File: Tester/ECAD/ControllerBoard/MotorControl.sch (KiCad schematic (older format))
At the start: 16 parts, among them J2 Conn_01x02_Male, J3 Conn_01x02_Male, J4 Conn_01x02_Male, J5 Conn_01x02_Male, U3 DRV8833PW, U4 DRV8833PW

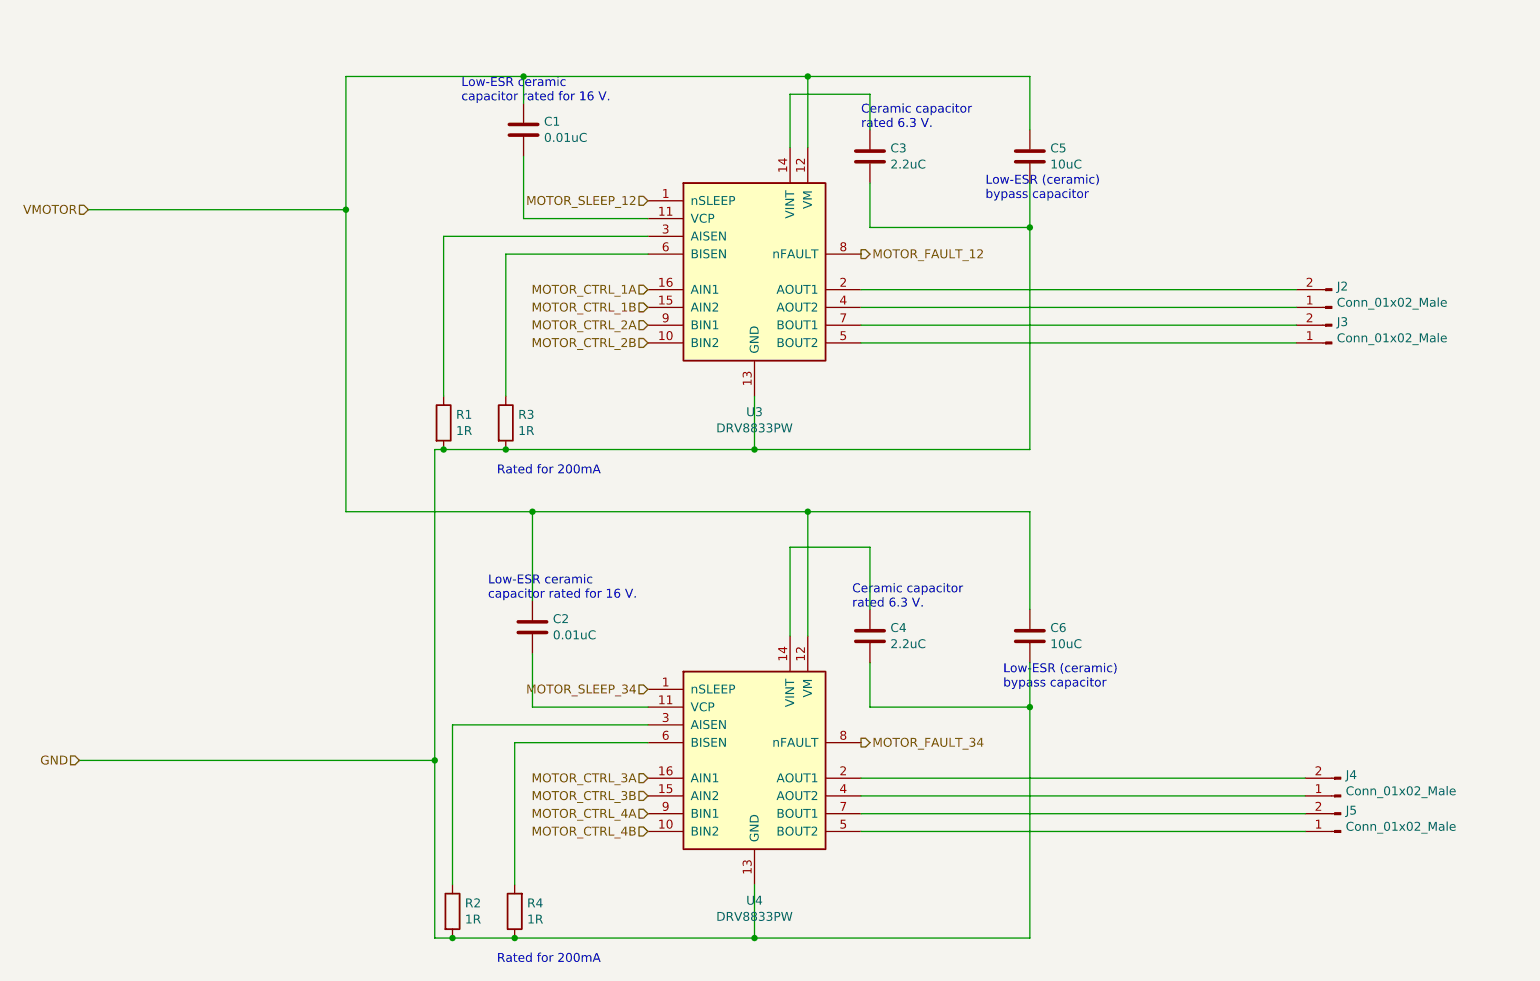
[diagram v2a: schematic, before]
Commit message: Progressed circuit layout.
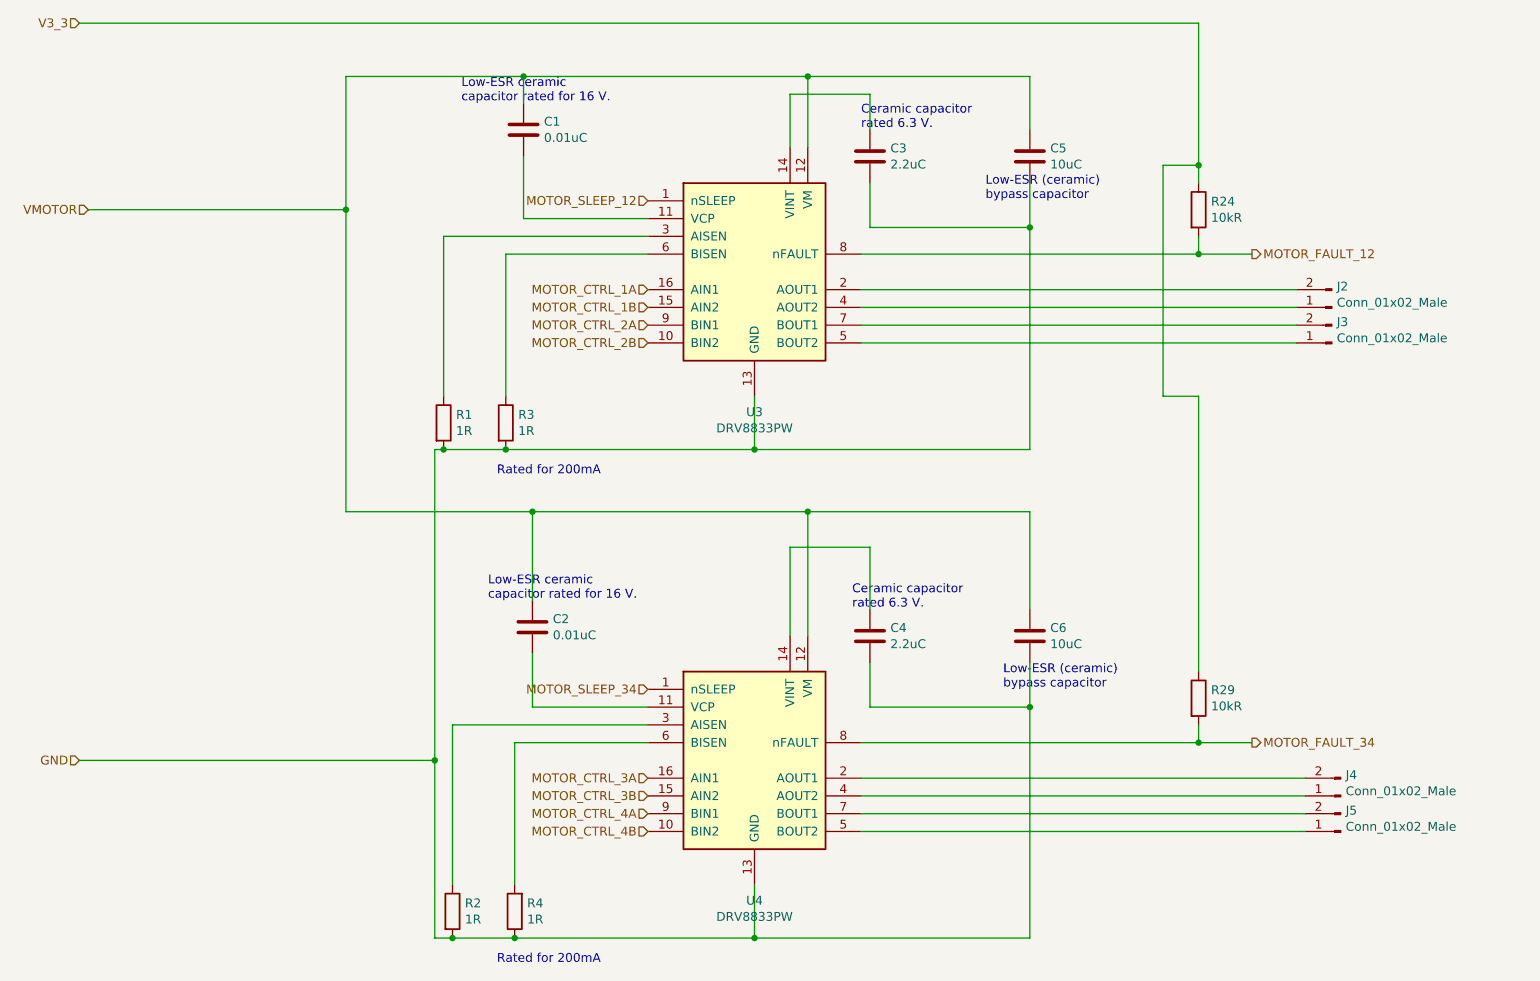
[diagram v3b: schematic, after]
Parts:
- added R24, R29: 10kR, Resistor_SMD:R_0805_2012Metric_Pad1.15x1.40mm_HandSolder, symbol Device:R
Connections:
- net MOTOR_FAULT_12: now also R24.2
- net MOTOR_FAULT_34: now also R29.2
- new net V3_3: R24.1, R29.1
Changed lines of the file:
@@
 Text Notes 6400 4200 0    50   ~ 0
 Ceramic capacitor\nrated 6.3 V.
-Text HLabel 6450 2200 2    50   Output ~ 0
+Text HLabel 8650 2200 2    50   Output ~ 0
 MOTOR_FAULT_12
-Text HLabel 6450 4950 2    50   Output ~ 0
+Text HLabel 8650 4950 2    50   Output ~ 0
 MOTOR_FAULT_34
 Text HLabel 5250 1900 0    50   Input ~ 0
@@
 Wire Wire Line
 	8950 5450 6450 5450
+$Comp
+L Device:R R29
+U 1 1 5E624B95
+P 8350 4700
+F 0 "R29" H 8420 4746 50  0000 L CNN
+F 1 "10kR" H 8420 4655 50  0000 L CNN
+F 2 "Resistor_SMD:R_0805_2012Metric_Pad1.15x1.40mm_HandSolder" V 8280 4700 50  0001 C CNN
+F 3 "~" H 8350 4700 50  0001 C CNN
+F 4 "RC0805FR-0710KL" H 8350 4700 50  0001 C CNN "Manufacturer Part Number"
+	1    8350 4700
+	1    0    0    -1
+$EndComp
+Wire Wire Line
+	6450 4950 8350 4950
+Wire Wire Line
+	8350 4850 8350 4950
+Connection ~ 8350 4950
+Wire Wire Line
+	8350 4950 8650 4950
+$Comp
+L Device:R R24
+U 1 1 5E6297EE
+P 8350 1950
+F 0 "R24" H 8420 1996 50  0000 L CNN
+F 1 "10kR" H 8420 1905 50  0000 L CNN
+F 2 "Resistor_SMD:R_0805_2012Metric_Pad1.15x1.40mm_HandSolder" V 8280 1950 50  0001 C CNN
+F 3 "~" H 8350 1950 50  0001 C CNN
+F 4 "RC0805FR-0710KL" H 8350 1950 50  0001 C CNN "Manufacturer Part Number"
+	1    8350 1950
+	1    0    0    -1
+$EndComp
+Wire Wire Line
+	6450 2200 8350 2200
+Wire Wire Line
+	8350 2100 8350 2200
+Connection ~ 8350 2200
+Wire Wire Line
+	8350 2200 8650 2200
+Text HLabel 2050 900  0    50   Input ~ 0
+V3_3
+Wire Wire Line
+	2050 900  8350 900
+Wire Wire Line
+	8350 900  8350 1700
+Wire Wire Line
+	8350 1700 8150 1700
+Wire Wire Line
+	8150 1700 8150 3000
+Wire Wire Line
+	8150 3000 8350 3000
+Wire Wire Line
+	8350 3000 8350 4550
+Connection ~ 8350 1700
+Wire Wire Line
+	8350 1700 8350 1800
 $EndSCHEMATC

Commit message: Progressed circuit layout.
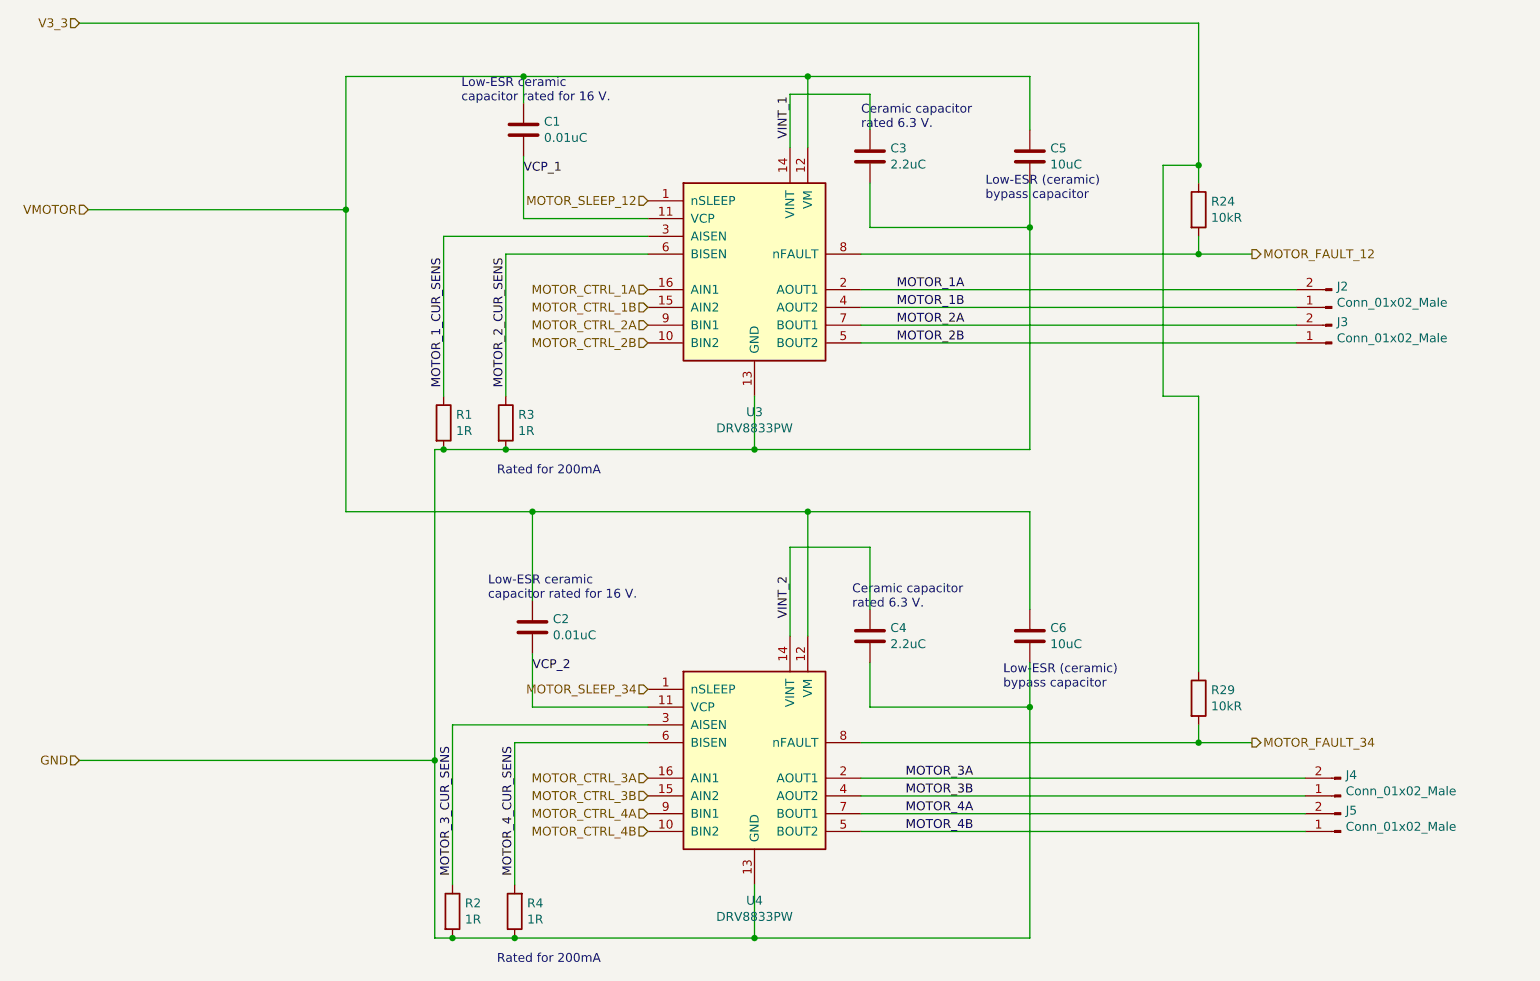
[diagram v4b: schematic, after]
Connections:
- net VCP_2: now reaches C2.2, U4.11 (VCP)
- net VINT_2: now reaches C4.1, U4.14 (VINT)
- net MOTOR_3A: now reaches J4.2 (Pin_2), U4.2 (AOUT1)
- net MOTOR_3_CUR_SENS: now reaches R2.1, U4.3 (AISEN)
- net MOTOR_3B: now reaches J4.1 (Pin_1), U4.4 (AOUT2)
- net MOTOR_4B: now reaches J5.1 (Pin_1), U4.5 (BOUT2)
- net MOTOR_4_CUR_SENS: now reaches R4.2, U4.6 (BISEN)
- net MOTOR_4A: now reaches J5.2 (Pin_2), U4.7 (BOUT1)
- net VCP_1: now reaches C1.2, U3.11 (VCP)
- net VINT_1: now reaches C3.1, U3.14 (VINT)
- net MOTOR_1A: now reaches J2.2 (Pin_2), U3.2 (AOUT1)
- net MOTOR_1_CUR_SENS: now reaches R1.1, U3.3 (AISEN)
- net MOTOR_1B: now reaches J2.1 (Pin_1), U3.4 (AOUT2)
- net MOTOR_2B: now reaches J3.1 (Pin_1), U3.5 (BOUT2)
- net MOTOR_2_CUR_SENS: now reaches R3.1, U3.6 (BISEN)
- net MOTOR_2A: now reaches J3.2 (Pin_2), U3.7 (BOUT1)
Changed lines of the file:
@@
 Wire Wire Line
 	8350 1700 8350 1800
+Text Label 6650 2400 0    50   ~ 0
+MOTOR_1A
+Text Label 6650 2500 0    50   ~ 0
+MOTOR_1B
+Text Label 6650 2600 0    50   ~ 0
+MOTOR_2A
+Text Label 6650 2700 0    50   ~ 0
+MOTOR_2B
+Text Label 6700 5150 0    50   ~ 0
+MOTOR_3A
+Text Label 6700 5250 0    50   ~ 0
+MOTOR_3B
+Text Label 6700 5350 0    50   ~ 0
+MOTOR_4A
+Text Label 6700 5450 0    50   ~ 0
+MOTOR_4B
+Text Label 4100 2950 1    50   ~ 0
+MOTOR_1_CUR_SENS
+Text Label 4450 2950 1    50   ~ 0
+MOTOR_2_CUR_SENS
+Text Label 4150 5700 1    50   ~ 0
+MOTOR_3_CUR_SENS
+Text Label 4500 5700 1    50   ~ 0
+MOTOR_4_CUR_SENS
+Text Label 6050 1550 1    50   ~ 0
+VINT_1
+Text Label 6050 4250 1    50   ~ 0
+VINT_2
+Text Label 4600 4550 0    50   ~ 0
+VCP_2
+Text Label 4550 1750 0    50   ~ 0
+VCP_1
 $EndSCHEMATC

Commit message: Added missing 3d models.
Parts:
- J2, J3, J4, J5: footprint Connector_Molex:Molex_PicoBlade_53048-0210_1x02_P1.25mm_Horizontal -> Connector_Molex_Custom:Molex_PicoBlade_53048-0210_1x02_P1.25mm_Horizontal
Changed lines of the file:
@@
 F 0 "J2" H 9072 2382 50  0000 R CNN
 F 1 "Conn_01x02_Male" H 9072 2473 50  0000 R CNN
-F 2 "Connector_Molex:Molex_PicoBlade_53048-0210_1x02_P1.25mm_Horizontal" H 9100 2500 50  0001 C CNN
+F 2 "Connector_Molex_Custom:Molex_PicoBlade_53048-0210_1x02_P1.25mm_Horizontal" H 9100 2500 50  0001 C CNN
 F 3 "~" H 9100 2500 50  0001 C CNN
 F 4 "0530480210" H 9100 2500 50  0001 C CNN "Manufacturer Part Number"
@@
 F 0 "J3" H 9072 2582 50  0000 R CNN
 F 1 "Conn_01x02_Male" H 9072 2673 50  0000 R CNN
-F 2 "Connector_Molex:Molex_PicoBlade_53048-0210_1x02_P1.25mm_Horizontal" H 9100 2700 50  0001 C CNN
+F 2 "Connector_Molex_Custom:Molex_PicoBlade_53048-0210_1x02_P1.25mm_Horizontal" H 9100 2700 50  0001 C CNN
 F 3 "~" H 9100 2700 50  0001 C CNN
 F 4 "0530480210" H 9100 2700 50  0001 C CNN "Manufacturer Part Number"
@@
 F 0 "J4" H 9122 5132 50  0000 R CNN
 F 1 "Conn_01x02_Male" H 9122 5223 50  0000 R CNN
-F 2 "Connector_Molex:Molex_PicoBlade_53048-0210_1x02_P1.25mm_Horizontal" H 9150 5250 50  0001 C CNN
+F 2 "Connector_Molex_Custom:Molex_PicoBlade_53048-0210_1x02_P1.25mm_Horizontal" H 9150 5250 50  0001 C CNN
 F 3 "~" H 9150 5250 50  0001 C CNN
 F 4 "0530480210" H 9150 5250 50  0001 C CNN "Manufacturer Part Number"
@@
 F 0 "J5" H 9122 5332 50  0000 R CNN
 F 1 "Conn_01x02_Male" H 9122 5423 50  0000 R CNN
-F 2 "Connector_Molex:Molex_PicoBlade_53048-0210_1x02_P1.25mm_Horizontal" H 9150 5450 50  0001 C CNN
+F 2 "Connector_Molex_Custom:Molex_PicoBlade_53048-0210_1x02_P1.25mm_Horizontal" H 9150 5450 50  0001 C CNN
 F 3 "~" H 9150 5450 50  0001 C CNN
 F 4 "0530480210" H 9150 5450 50  0001 C CNN "Manufacturer Part Number"

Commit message: Progressed circuit layout.
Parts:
- J2, J3, J4, J5: footprint Connector_Molex_Custom:Molex_PicoBlade_53048-0210_1x02_P1.25mm_Horizontal -> (none); Manufacturer Part Number 0530480210 -> (none)
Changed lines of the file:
@@
 $Descr A4 11693 8268
 encoding utf-8
-Sheet 2 6
+Sheet 2 7
 Title ""
 Date ""
@@
 F 0 "J2" H 9072 2382 50  0000 R CNN
 F 1 "Conn_01x02_Male" H 9072 2473 50  0000 R CNN
-F 2 "Connector_Molex_Custom:Molex_PicoBlade_53048-0210_1x02_P1.25mm_Horizontal" H 9100 2500 50  0001 C CNN
+F 2 "" H 9100 2500 50  0001 C CNN
 F 3 "~" H 9100 2500 50  0001 C CNN
-F 4 "0530480210" H 9100 2500 50  0001 C CNN "Manufacturer Part Number"
+F 4 "" H 9100 2500 50  0001 C CNN "Manufacturer Part Number"
 	1    9100 2500
 	-1   0    0    1
@@
 F 0 "J3" H 9072 2582 50  0000 R CNN
 F 1 "Conn_01x02_Male" H 9072 2673 50  0000 R CNN
-F 2 "Connector_Molex_Custom:Molex_PicoBlade_53048-0210_1x02_P1.25mm_Horizontal" H 9100 2700 50  0001 C CNN
+F 2 "" H 9100 2700 50  0001 C CNN
 F 3 "~" H 9100 2700 50  0001 C CNN
-F 4 "0530480210" H 9100 2700 50  0001 C CNN "Manufacturer Part Number"
+F 4 "" H 9100 2700 50  0001 C CNN "Manufacturer Part Number"
 	1    9100 2700
 	-1   0    0    1
@@
 F 0 "J4" H 9122 5132 50  0000 R CNN
 F 1 "Conn_01x02_Male" H 9122 5223 50  0000 R CNN
-F 2 "Connector_Molex_Custom:Molex_PicoBlade_53048-0210_1x02_P1.25mm_Horizontal" H 9150 5250 50  0001 C CNN
+F 2 "" H 9150 5250 50  0001 C CNN
 F 3 "~" H 9150 5250 50  0001 C CNN
-F 4 "0530480210" H 9150 5250 50  0001 C CNN "Manufacturer Part Number"
+F 4 "" H 9150 5250 50  0001 C CNN "Manufacturer Part Number"
 	1    9150 5250
 	-1   0    0    1
@@
 F 0 "J5" H 9122 5332 50  0000 R CNN
 F 1 "Conn_01x02_Male" H 9122 5423 50  0000 R CNN
-F 2 "Connector_Molex_Custom:Molex_PicoBlade_53048-0210_1x02_P1.25mm_Horizontal" H 9150 5450 50  0001 C CNN
+F 2 "" H 9150 5450 50  0001 C CNN
 F 3 "~" H 9150 5450 50  0001 C CNN
-F 4 "0530480210" H 9150 5450 50  0001 C CNN "Manufacturer Part Number"
+F 4 "" H 9150 5450 50  0001 C CNN "Manufacturer Part Number"
 	1    9150 5450
 	-1   0    0    1

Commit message: Progressed circuit updates.
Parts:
- removed C2: 0.01uC, Capacitor_SMD:C_0805_2012Metric_Pad1.15x1.40mm_HandSolder, symbol Device:C
- removed C4: 2.2uC, Capacitor_SMD:C_0805_2012Metric_Pad1.15x1.40mm_HandSolder, symbol Device:C
- removed C6: 10uC, Capacitor_SMD:C_0805_2012Metric_Pad1.15x1.40mm_HandSolder, symbol Device:C
- removed J4, J5: Conn_01x02_Male, symbol Connector:Conn_01x02_Male
- removed R2, R4: 1R, Resistor_SMD:R_0805_2012Metric_Pad1.15x1.40mm_HandSolder, symbol Device:R
- removed R29: 10kR, Resistor_SMD:R_0805_2012Metric_Pad1.15x1.40mm_HandSolder, symbol Device:R
- removed U4: DRV8833PW, Package_SO:TSSOP-16_4.4x5mm_P0.65mm, symbol Driver_Motor:DRV8833PW
- added NT3: Net-Tie_2, symbol Device:Net-Tie_2
- J2, J3: footprint (none) -> Connector_JST:JST_XH_B2B-XH-A_1x02_P2.50mm_Vertical; Manufacturer Part Number (none) -> B2B-XH-A(LF)(SN)
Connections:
- net VMOTOR: no longer names the net of C1.1, C5.1, U3.12 (VM)
- net VMOTOR: now also NT3.2
- new net V5_0: NT3.1
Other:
- moved on the sheet: C1, C3, C5, J2, J3, R1, R24, R3, U3

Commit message: Progressed circuit layout.
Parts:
- NT3: footprint (none) -> NetTie:NetTie-2_SMD_Pad0.5mm
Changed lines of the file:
@@
 F 0 "NT3" H 3400 3081 50  0000 C CNN
 F 1 "Net-Tie_2" H 3400 2990 50  0000 C CNN
-F 2 "" H 3400 2900 50  0001 C CNN
+F 2 "NetTie:NetTie-2_SMD_Pad0.5mm" H 3400 2900 50  0001 C CNN
 F 3 "~" H 3400 2900 50  0001 C CNN
 	1    3400 2900
